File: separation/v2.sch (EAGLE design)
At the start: 11 parts

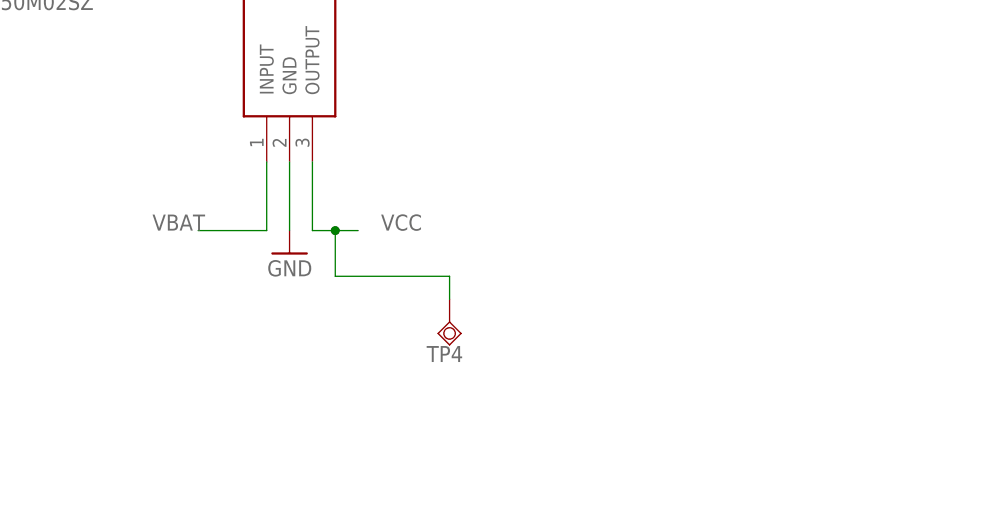
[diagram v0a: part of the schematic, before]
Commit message: add headers to use second i2c bus if required
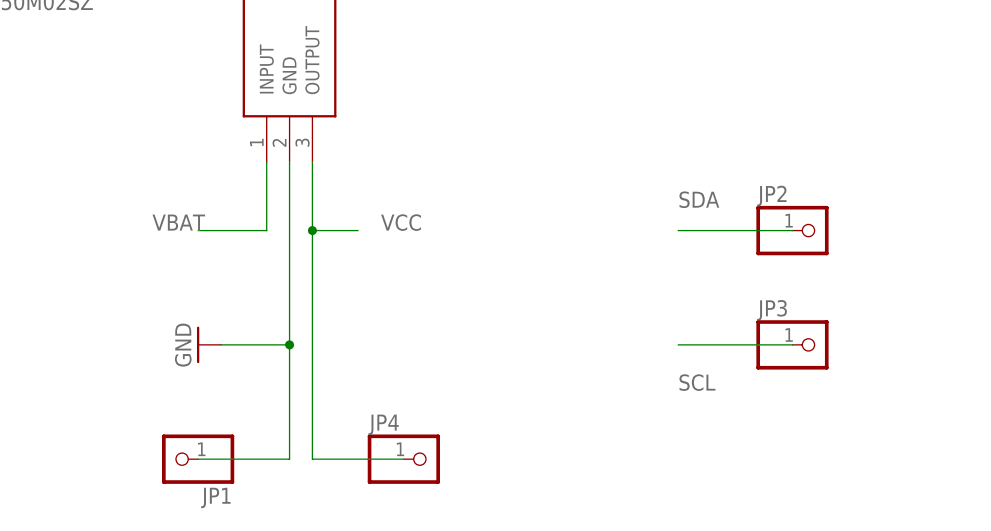
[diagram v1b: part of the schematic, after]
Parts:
- removed TP4: TPSQB2,54, testpad:TPSQB2,54
- added JP1, JP2, JP3, JP4: (no value), pinhead:PINHD-1X1
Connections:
- net GND: now also JP1.1
- net SCL: now also JP3.1
- net SDA: now also JP2.1
- net VCC: now also JP4.1; no longer TP4.TP
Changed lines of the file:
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@@
 <part name="GND6" library="supply1" library_urn="urn:adsk.eagle:library:371" deviceset="GND" device=""/>
 <part name="TP2" library="testpad" library_urn="urn:adsk.eagle:library:385" deviceset="TPSQ" device="B2,54" package3d_urn="urn:adsk.eagle:package:27948/1"/>
-<part name="TP4" library="testpad" library_urn="urn:adsk.eagle:library:385" deviceset="TPSQ" device="B2,54" package3d_urn="urn:adsk.eagle:package:27948/1"/>
 <part name="TP6" library="testpad" library_urn="urn:adsk.eagle:library:385" deviceset="TPSQ" device="B2,54" package3d_urn="urn:adsk.eagle:package:27948/1"/>
+<part name="JP2" library="pinhead" library_urn="urn:adsk.eagle:library:325" deviceset="PINHD-1X1" device="" package3d_urn="urn:adsk.eagle:package:22485/2"/>
+<part name="JP3" library="pinhead" library_urn="urn:adsk.eagle:library:325" deviceset="PINHD-1X1" device="" package3d_urn="urn:adsk.eagle:package:22485/2"/>
+<part name="JP1" library="pinhead" library_urn="urn:adsk.eagle:library:325" deviceset="PINHD-1X1" device="" package3d_urn="urn:adsk.eagle:package:22485/2"/>
+<part name="JP4" library="pinhead" library_urn="urn:adsk.eagle:library:325" deviceset="PINHD-1X1" device="" package3d_urn="urn:adsk.eagle:package:22485/2"/>
 </parts>
 <sheets>
@@
 <attribute name="VALUE" x="-30.48" y="5.08" size="1.778" layer="96" rot="MR90"/>
 </instance>
-<instance part="GND4" gate="1" x="43.18" y="-12.7" smashed="yes" rot="MR0">
-<attribute name="VALUE" x="45.72" y="-15.24" size="1.778" layer="96" rot="MR0"/>
+<instance part="GND4" gate="1" x="33.02" y="-22.86" smashed="yes" rot="MR90">
+<attribute name="VALUE" x="30.48" y="-25.4" size="1.778" layer="96" rot="MR90"/>
 </instance>
 <instance part="GND5" gate="1" x="106.68" y="35.56" smashed="yes" rot="MR90">
@@
 <attribute name="TP_SIGNAL_NAME" x="-7.62" y="-31.75" size="1.778" layer="97"/>
 </instance>
-<instance part="TP4" gate="G$1" x="60.96" y="-20.32" smashed="yes">
-<attribute name="NAME" x="58.42" y="-24.765" size="1.778" layer="95"/>
-<attribute name="TP_SIGNAL_NAME" x="63.5" y="-21.59" size="1.778" layer="97"/>
-</instance>
 <instance part="TP6" gate="G$1" x="114.3" y="58.42" smashed="yes" rot="R180">
 <attribute name="NAME" x="116.84" y="62.865" size="1.778" layer="95" rot="R180"/>
 <attribute name="TP_SIGNAL_NAME" x="111.76" y="59.69" size="1.778" layer="97" rot="R180"/>
+</instance>
+<instance part="JP2" gate="G$1" x="101.6" y="-10.16" smashed="yes">
+<attribute name="NAME" x="95.25" y="-6.985" size="1.778" layer="95"/>
+<attribute name="VALUE" x="95.25" y="-15.24" size="1.778" layer="96"/>
+</instance>
+<instance part="JP3" gate="G$1" x="101.6" y="-22.86" smashed="yes">
+<attribute name="NAME" x="95.25" y="-19.685" size="1.778" layer="95"/>
+<attribute name="VALUE" x="95.25" y="-27.94" size="1.778" layer="96"/>
+</instance>
+<instance part="JP1" gate="G$1" x="30.48" y="-35.56" smashed="yes" rot="R180">
+<attribute name="NAME" x="36.83" y="-38.735" size="1.778" layer="95" rot="R180"/>
+<attribute name="VALUE" x="36.83" y="-30.48" size="1.778" layer="96" rot="R180"/>
+</instance>
+<instance part="JP4" gate="G$1" x="58.42" y="-35.56" smashed="yes">
+<attribute name="NAME" x="52.07" y="-32.385" size="1.778" layer="95"/>
+<attribute name="VALUE" x="52.07" y="-40.64" size="1.778" layer="96"/>
 </instance>
 </instances>
@@
 </segment>
 <segment>
-<pinref part="GND4" gate="1" pin="GND"/>
-<pinref part="LDO" gate="G$1" pin="GND"/>
-<wire x1="43.18" y1="-10.16" x2="43.18" y2="-2.54" width="0.1524" layer="91"/>
-</segment>
-<segment>
 <pinref part="GND5" gate="1" pin="GND"/>
 <pinref part="LOUD" gate="G$1" pin="-"/>
@@
 <wire x1="-17.78" y1="40.64" x2="-17.78" y2="45.72" width="0.1524" layer="91"/>
 </segment>
+<segment>
+<pinref part="LDO" gate="G$1" pin="GND"/>
+<wire x1="43.18" y1="-2.54" x2="43.18" y2="-22.86" width="0.1524" layer="91"/>
+<pinref part="GND4" gate="1" pin="GND"/>
+<wire x1="43.18" y1="-22.86" x2="43.18" y2="-35.56" width="0.1524" layer="91"/>
+<wire x1="35.56" y1="-22.86" x2="43.18" y2="-22.86" width="0.1524" layer="91"/>
+<junction x="43.18" y="-22.86"/>
+<pinref part="JP1" gate="G$1" pin="1"/>
+<wire x1="43.18" y1="-35.56" x2="33.02" y2="-35.56" width="0.1524" layer="91"/>
+</segment>
 </net>
 <net name="MOSI" class="0">
@@
 <label x="45.72" y="53.34" size="1.778" layer="95"/>
 </segment>
+<segment>
+<pinref part="JP3" gate="G$1" pin="1"/>
+<wire x1="99.06" y1="-22.86" x2="86.36" y2="-22.86" width="0.1524" layer="91"/>
+<label x="86.36" y="-27.94" size="1.778" layer="95"/>
+</segment>
 </net>
 <net name="SDA" class="0">
@@
 <wire x1="45.72" y1="55.88" x2="58.42" y2="55.88" width="0.1524" layer="91"/>
 <label x="45.72" y="55.88" size="1.778" layer="95"/>
+</segment>
+<segment>
+<pinref part="JP2" gate="G$1" pin="1"/>
+<wire x1="99.06" y1="-10.16" x2="86.36" y2="-10.16" width="0.1524" layer="91"/>
+<label x="86.36" y="-7.62" size="1.778" layer="95"/>
 </segment>
 </net>
@@
 <pinref part="LDO" gate="G$1" pin="OUTPUT"/>
 <wire x1="45.72" y1="-2.54" x2="45.72" y2="-10.16" width="0.1524" layer="91"/>
-<wire x1="45.72" y1="-10.16" x2="48.26" y2="-10.16" width="0.1524" layer="91"/>
 <label x="53.34" y="-10.16" size="1.778" layer="95"/>
-<pinref part="TP4" gate="G$1" pin="TP"/>
-<wire x1="48.26" y1="-10.16" x2="50.8" y2="-10.16" width="0.1524" layer="91"/>
-<wire x1="60.96" y1="-17.78" x2="60.96" y2="-15.24" width="0.1524" layer="91"/>
-<wire x1="60.96" y1="-15.24" x2="48.26" y2="-15.24" width="0.1524" layer="91"/>
-<wire x1="48.26" y1="-15.24" x2="48.26" y2="-10.16" width="0.1524" layer="91"/>
-<junction x="48.26" y="-10.16"/>
-</segment>
-</net>
+<wire x1="45.72" y1="-10.16" x2="50.8" y2="-10.16" width="0.1524" layer="91"/>
+<junction x="45.72" y="-10.16"/>
+<wire x1="45.72" y1="-10.16" x2="45.72" y2="-35.56" width="0.1524" layer="91"/>
+<pinref part="JP4" gate="G$1" pin="1"/>
+<wire x1="45.72" y1="-35.56" x2="55.88" y2="-35.56" width="0.1524" layer="91"/>
+</segment>
+</net>

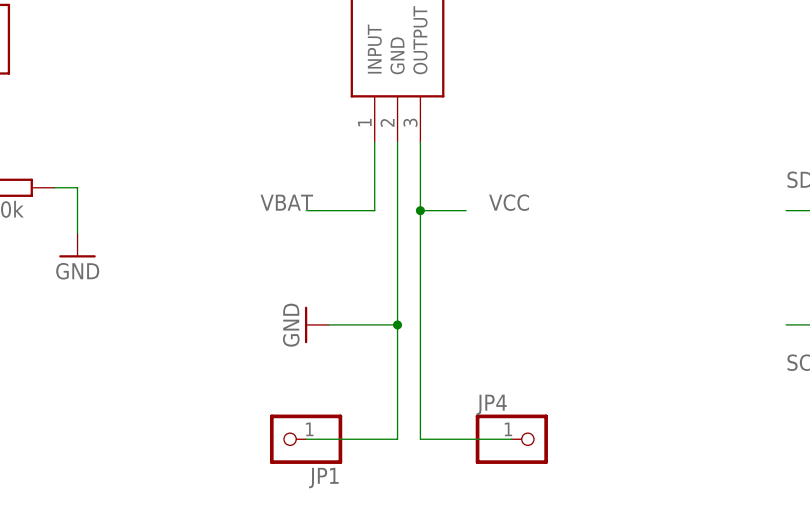
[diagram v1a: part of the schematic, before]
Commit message: add 2x caps for regulator
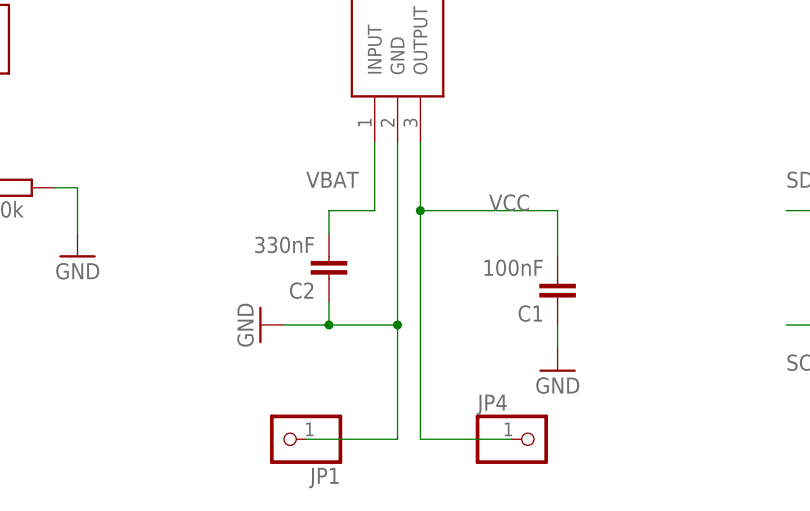
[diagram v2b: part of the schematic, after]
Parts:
- added C1: 100nF, rcl:C-EU025-024X044
- added C2: 330nF, rcl:C-EU025-024X044
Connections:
- net GND: now also C1.1, C2.1
- net VBAT: now also C2.2
- net VCC: now also C1.2
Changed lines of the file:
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@@
 <part name="JP1" library="pinhead" library_urn="urn:adsk.eagle:library:325" deviceset="PINHD-1X1" device="" package3d_urn="urn:adsk.eagle:package:22485/2"/>
 <part name="JP4" library="pinhead" library_urn="urn:adsk.eagle:library:325" deviceset="PINHD-1X1" device="" package3d_urn="urn:adsk.eagle:package:22485/2"/>
+<part name="C1" library="rcl" library_urn="urn:adsk.eagle:library:334" deviceset="C-EU" device="025-024X044" package3d_urn="urn:adsk.eagle:package:23630/1" value="100nF"/>
+<part name="C2" library="rcl" library_urn="urn:adsk.eagle:library:334" deviceset="C-EU" device="025-024X044" package3d_urn="urn:adsk.eagle:package:23630/1" value="330nF"/>
+<part name="GND7" library="supply1" library_urn="urn:adsk.eagle:library:371" deviceset="GND" device=""/>
 </parts>
 <sheets>
@@
 <attribute name="VALUE" x="-30.48" y="5.08" size="1.778" layer="96" rot="MR90"/>
 </instance>
-<instance part="GND4" gate="1" x="33.02" y="-22.86" smashed="yes" rot="MR90">
-<attribute name="VALUE" x="30.48" y="-25.4" size="1.778" layer="96" rot="MR90"/>
+<instance part="GND4" gate="1" x="27.94" y="-22.86" smashed="yes" rot="MR90">
+<attribute name="VALUE" x="25.4" y="-25.4" size="1.778" layer="96" rot="MR90"/>
 </instance>
 <instance part="GND5" gate="1" x="106.68" y="35.56" smashed="yes" rot="MR90">
@@
 <attribute name="NAME" x="52.07" y="-32.385" size="1.778" layer="95"/>
 <attribute name="VALUE" x="52.07" y="-40.64" size="1.778" layer="96"/>
+</instance>
+<instance part="C1" gate="G$1" x="60.96" y="-20.32" smashed="yes" rot="R180">
+<attribute name="NAME" x="59.436" y="-20.701" size="1.778" layer="95" rot="R180"/>
+<attribute name="VALUE" x="59.436" y="-15.621" size="1.778" layer="96" rot="R180"/>
+</instance>
+<instance part="C2" gate="G$1" x="35.56" y="-17.78" smashed="yes" rot="R180">
+<attribute name="NAME" x="34.036" y="-18.161" size="1.778" layer="95" rot="R180"/>
+<attribute name="VALUE" x="34.036" y="-13.081" size="1.778" layer="96" rot="R180"/>
+</instance>
+<instance part="GND7" gate="1" x="60.96" y="-27.94" smashed="yes" rot="MR0">
+<attribute name="VALUE" x="63.5" y="-30.48" size="1.778" layer="96" rot="MR0"/>
 </instance>
 </instances>
@@
 <pinref part="GND4" gate="1" pin="GND"/>
 <wire x1="43.18" y1="-22.86" x2="43.18" y2="-35.56" width="0.1524" layer="91"/>
-<wire x1="35.56" y1="-22.86" x2="43.18" y2="-22.86" width="0.1524" layer="91"/>
+<wire x1="30.48" y1="-22.86" x2="35.56" y2="-22.86" width="0.1524" layer="91"/>
 <junction x="43.18" y="-22.86"/>
 <pinref part="JP1" gate="G$1" pin="1"/>
+<wire x1="35.56" y1="-22.86" x2="43.18" y2="-22.86" width="0.1524" layer="91"/>
 <wire x1="43.18" y1="-35.56" x2="33.02" y2="-35.56" width="0.1524" layer="91"/>
+<pinref part="C2" gate="G$1" pin="1"/>
+<wire x1="35.56" y1="-20.32" x2="35.56" y2="-22.86" width="0.1524" layer="91"/>
+<junction x="35.56" y="-22.86"/>
+</segment>
+<segment>
+<pinref part="GND7" gate="1" pin="GND"/>
+<wire x1="60.96" y1="-25.4" x2="60.96" y2="-22.86" width="0.1524" layer="91"/>
+<pinref part="C1" gate="G$1" pin="1"/>
 </segment>
 </net>
@@
 <wire x1="45.72" y1="-2.54" x2="45.72" y2="-10.16" width="0.1524" layer="91"/>
 <label x="53.34" y="-10.16" size="1.778" layer="95"/>
-<wire x1="45.72" y1="-10.16" x2="50.8" y2="-10.16" width="0.1524" layer="91"/>
 <junction x="45.72" y="-10.16"/>
 <wire x1="45.72" y1="-10.16" x2="45.72" y2="-35.56" width="0.1524" layer="91"/>
 <pinref part="JP4" gate="G$1" pin="1"/>
 <wire x1="45.72" y1="-35.56" x2="55.88" y2="-35.56" width="0.1524" layer="91"/>
+<wire x1="45.72" y1="-10.16" x2="60.96" y2="-10.16" width="0.1524" layer="91"/>
+<pinref part="C1" gate="G$1" pin="2"/>
+<wire x1="60.96" y1="-10.16" x2="60.96" y2="-15.24" width="0.1524" layer="91"/>
 </segment>
 </net>
@@
 <pinref part="LDO" gate="G$1" pin="INPUT"/>
 <wire x1="40.64" y1="-2.54" x2="40.64" y2="-10.16" width="0.1524" layer="91"/>
-<wire x1="40.64" y1="-10.16" x2="33.02" y2="-10.16" width="0.1524" layer="91"/>
-<label x="27.94" y="-10.16" size="1.778" layer="95"/>
-</segment>
-<segment>
+<wire x1="40.64" y1="-10.16" x2="35.56" y2="-10.16" width="0.1524" layer="91"/>
+<label x="33.02" y="-7.62" size="1.778" layer="95"/>
+<pinref part="C2" gate="G$1" pin="2"/>
+<wire x1="35.56" y1="-12.7" x2="35.56" y2="-10.16" width="0.1524" layer="91"/>
+</segment>
+<segment>

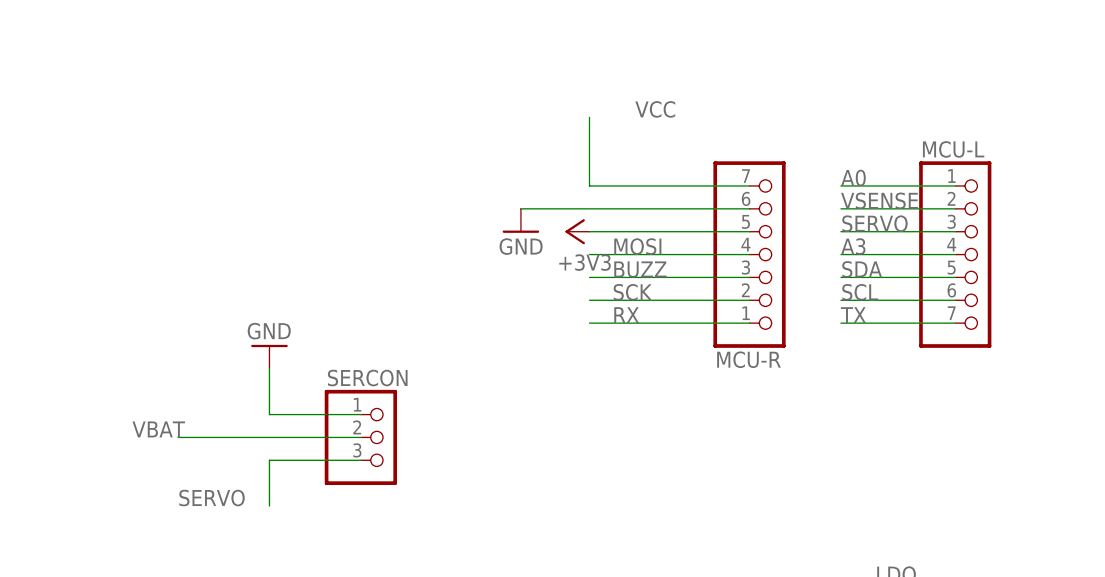
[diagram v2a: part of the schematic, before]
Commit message: connect mosfet in schematic
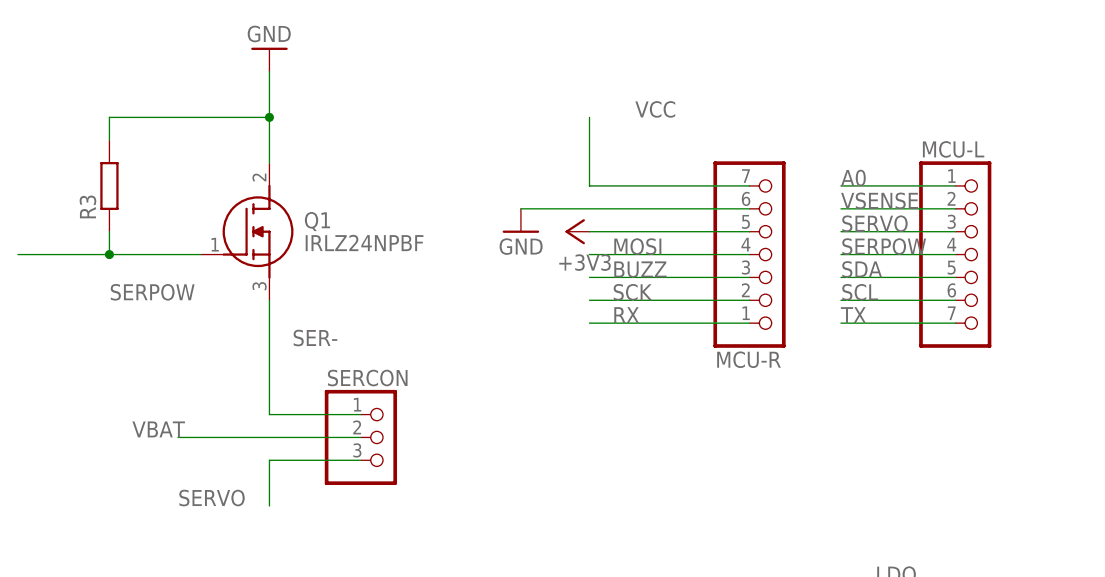
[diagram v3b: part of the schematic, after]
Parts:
- added Q1: IRLZ24NPBF, SamacSys_Parts:IRLZ24NPBF
- added R3: (no value), rcl:R-EU_0204/2V
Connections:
- removed net A3: MCU-L.4
- new net SER-: Q1.S, SERCON.1
- new net SERPOW: MCU-L.4, Q1.G, R3.1
- net GND: now also Q1.D, R3.2; no longer SERCON.1
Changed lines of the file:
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@@
 <part name="C2" library="rcl" library_urn="urn:adsk.eagle:library:334" deviceset="C-EU" device="025-024X044" package3d_urn="urn:adsk.eagle:package:23630/1" value="330nF"/>
 <part name="GND7" library="supply1" library_urn="urn:adsk.eagle:library:371" deviceset="GND" device=""/>
+<part name="Q1" library="SamacSys_Parts" deviceset="IRLZ24NPBF" device=""/>
+<part name="R3" library="rcl" library_urn="urn:adsk.eagle:library:334" deviceset="R-EU_" device="0204/2V" package3d_urn="urn:adsk.eagle:package:23495/1"/>
 </parts>
 <sheets>
@@
 <attribute name="VALUE" x="-11.43" y="30.48" size="1.778" layer="96"/>
 </instance>
-<instance part="GND2" gate="1" x="-17.78" y="48.26" smashed="yes" rot="MR180">
-<attribute name="VALUE" x="-20.32" y="50.8" size="1.778" layer="96" rot="MR180"/>
+<instance part="GND2" gate="1" x="-17.78" y="81.28" smashed="yes" rot="MR180">
+<attribute name="VALUE" x="-20.32" y="83.82" size="1.778" layer="96" rot="MR180"/>
 </instance>
 <instance part="GND3" gate="1" x="-27.94" y="7.62" smashed="yes" rot="MR90">
@@
 <instance part="GND7" gate="1" x="60.96" y="-27.94" smashed="yes" rot="MR0">
 <attribute name="VALUE" x="63.5" y="-30.48" size="1.778" layer="96" rot="MR0"/>
+</instance>
+<instance part="Q1" gate="G$1" x="-25.4" y="58.42" smashed="yes">
+<attribute name="NAME" x="-13.97" y="62.23" size="1.778" layer="95" align="center-left"/>
+<attribute name="VALUE" x="-13.97" y="59.69" size="1.778" layer="96" align="center-left"/>
+</instance>
+<instance part="R3" gate="G$1" x="-35.56" y="66.04" smashed="yes" rot="R90">
+<attribute name="NAME" x="-37.0586" y="62.23" size="1.778" layer="95" rot="R90"/>
+<attribute name="VALUE" x="-32.258" y="62.23" size="1.778" layer="96" rot="R90"/>
 </instance>
 </instances>
@@
 <wire x1="5.08" y1="-7.62" x2="7.62" y2="-7.62" width="0.1524" layer="91"/>
 <wire x1="7.62" y1="-7.62" x2="7.62" y2="-12.7" width="0.1524" layer="91"/>
-</segment>
-<segment>
-<pinref part="SERCON" gate="A" pin="1"/>
-<wire x1="-7.62" y1="40.64" x2="-17.78" y2="40.64" width="0.1524" layer="91"/>
-<pinref part="GND2" gate="1" pin="GND"/>
-<wire x1="-17.78" y1="40.64" x2="-17.78" y2="45.72" width="0.1524" layer="91"/>
 </segment>
 <segment>
@@
 <pinref part="C1" gate="G$1" pin="1"/>
 </segment>
+<segment>
+<pinref part="Q1" gate="G$1" pin="D"/>
+<pinref part="GND2" gate="1" pin="GND"/>
+<wire x1="-17.78" y1="68.58" x2="-17.78" y2="73.66" width="0.1524" layer="91"/>
+<pinref part="R3" gate="G$1" pin="2"/>
+<wire x1="-17.78" y1="73.66" x2="-17.78" y2="78.74" width="0.1524" layer="91"/>
+<wire x1="-35.56" y1="71.12" x2="-35.56" y2="73.66" width="0.1524" layer="91"/>
+<wire x1="-35.56" y1="73.66" x2="-17.78" y2="73.66" width="0.1524" layer="91"/>
+<junction x="-17.78" y="73.66"/>
+</segment>
 </net>
 <net name="MOSI" class="0">
@@
 <label x="20.32" y="53.34" size="1.778" layer="95"/>
 <pinref part="MCU-R" gate="A" pin="2"/>
-</segment>
-</net>
-<net name="A3" class="0">
-<segment>
-<label x="45.72" y="58.42" size="1.778" layer="95"/>
-<pinref part="MCU-L" gate="A" pin="4"/>
-<wire x1="58.42" y1="58.42" x2="45.72" y2="58.42" width="0.1524" layer="91"/>
 </segment>
 </net>
@@
 </segment>
 </net>
+<net name="SER-" class="1">
+<segment>
+<pinref part="SERCON" gate="A" pin="1"/>
+<wire x1="-7.62" y1="40.64" x2="-17.78" y2="40.64" width="0.1524" layer="91"/>
+<pinref part="Q1" gate="G$1" pin="S"/>
+<wire x1="-17.78" y1="40.64" x2="-17.78" y2="53.34" width="0.1524" layer="91"/>
+<label x="-15.24" y="48.26" size="1.778" layer="95"/>
+</segment>
+</net>
+<net name="SERPOW" class="0">
+<segment>
+<pinref part="Q1" gate="G$1" pin="G"/>
+<wire x1="-25.4" y1="58.42" x2="-35.56" y2="58.42" width="0.1524" layer="91"/>
+<label x="-35.56" y="53.34" size="1.778" layer="95"/>
+<pinref part="R3" gate="G$1" pin="1"/>
+<wire x1="-35.56" y1="60.96" x2="-35.56" y2="58.42" width="0.1524" layer="91"/>
+<wire x1="-35.56" y1="58.42" x2="-45.72" y2="58.42" width="0.1524" layer="91"/>
+<junction x="-35.56" y="58.42"/>
+</segment>
+<segment>
+<label x="45.72" y="58.42" size="1.778" layer="95"/>
+<pinref part="MCU-L" gate="A" pin="4"/>
+<wire x1="58.42" y1="58.42" x2="45.72" y2="58.42" width="0.1524" layer="91"/>
+</segment>
+</net>
